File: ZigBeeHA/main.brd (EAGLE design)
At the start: 100 x 80 mm, 12 parts, among them IC1 REG1117

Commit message: 1st completion
1st completion
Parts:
- added F1: (no value), fuse:GSH15
- added PAD4, PAD5, PAD6: (no value), wirepad:2,54/0,8
- added PAD7: +5V, wirepad:2,54/0,8
- added PAD8: GND, wirepad:2,54/0,8
- added PAD9: +3.3V, wirepad:2,54/0,8
- added SV4: (no value), con-lstb:MA03-1
- added X1: 5202-03-N-02, con-ebyelectro:5202-03-N-02
- PAD1: value +5V -> AC-; device wirepad:2,54/0,8 -> wirepad:2,54/1,0
- PAD2: value GND -> AC+; device wirepad:2,54/0,8 -> wirepad:2,54/1,0
- PAD3: value +3.3V -> (none)
- moved PAD3 83.3 mm to (-6.35, -30.5)
- moved PAD2 75.5 mm to (-6.35, -20.3)
- moved PAD1 54.6 mm to (-6.35, -15.2)
- renumbered C5 to C4
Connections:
- new net AC+: X1.3
- new net LAMP: X1.2
- new net N$1: PAD1.1, PAD3.1
- new net N$2: F1.1, PAD2.1
- new net N$3: F1.2, PAD4.1
- net +5V: now also PAD5.1, PAD7.1, SV4.1; no longer PAD1.1
- net GND: now also PAD6.1, PAD8.1, SV4.2; no longer PAD2.1
- net PC6/MODE/DIO0: now also SV4.3
- net VCC: now also PAD9.1; no longer PAD3.1
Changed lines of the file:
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@@
 <element name="C3" library="rcl" package="SANYO-OSCON_SMD_A5" value="4.7uF" x="13.97" y="44.45" rot="R180"/>
 <element name="R1" library="rcl" package="M1206" value="10K" x="15.24" y="52.07" rot="R180"/>
-<element name="PAD1" library="wirepad" package="2,54/0,8" value="+5V" x="5.08" y="38.1"/>
-<element name="PAD2" library="wirepad" package="2,54/0,8" value="GND" x="60.96" y="13.97"/>
-<element name="PAD3" library="wirepad" package="2,54/0,8" value="+3.3V" x="5.08" y="52.07"/>
+<element name="PAD7" library="wirepad" package="2,54/0,8" value="+5V" x="5.08" y="38.1"/>
+<element name="PAD8" library="wirepad" package="2,54/0,8" value="GND" x="60.96" y="13.97"/>
+<element name="PAD9" library="wirepad" package="2,54/0,8" value="+3.3V" x="5.08" y="52.07"/>
 <element name="SV1" library="con-lstb" package="MA13-1" value="" x="35.56" y="36.83" rot="R270">
 <attribute name="OC_NEWARK" value="unknown" x="8.89" y="6.35" size="1.778" layer="27" rot="R270" display="off"/>
@@
 </element>
 <element name="C1" library="rcl" package="SANYO-OSCON_SMD_A5" value="4.7uF" x="21.59" y="27.94" rot="R90"/>
-<element name="C5" library="rcl" package="C1206" value="10uF" x="21.59" y="50.8" rot="R270"/>
+<element name="C4" library="rcl" package="C1206" value="10uF" x="21.59" y="50.8" rot="R270"/>
+<element name="F1" library="fuse" package="GSH15" value="" x="12.7" y="-6.35">
+<attribute name="OC_NEWARK" value="02P0318" x="12.7" y="-6.35" size="1.778" layer="27" display="off"/>
+<attribute name="MPN" value="64900001039" x="12.7" y="-6.35" size="1.778" layer="27" display="off"/>
+<attribute name="MF" value="" x="12.7" y="-6.35" size="1.778" layer="27" display="off"/>
+<attribute name="OC_FARNELL" value="1271673" x="12.7" y="-6.35" size="1.778" layer="27" display="off"/>
+</element>
+<element name="PAD1" library="wirepad" package="2,54/1,0" value="AC-" x="-6.35" y="-15.24"/>
+<element name="PAD2" library="wirepad" package="2,54/1,0" value="AC+" x="-6.35" y="-20.32"/>
+<element name="PAD3" library="wirepad" package="2,54/0,8" value="" x="-6.35" y="-30.48"/>
+<element name="PAD4" library="wirepad" package="2,54/0,8" value="" x="-6.35" y="-35.56"/>
+<element name="PAD5" library="wirepad" package="2,54/0,8" value="" x="-6.35" y="-40.64"/>
+<element name="PAD6" library="wirepad" package="2,54/0,8" value="" x="-6.35" y="-45.72"/>
+<element name="SV4" library="con-lstb" package="MA03-1" value="" x="-2.54" y="-50.8">
+<attribute name="OC_NEWARK" value="unknown" x="-2.54" y="-50.8" size="1.778" layer="27" display="off"/>
+<attribute name="MPN" value="" x="-2.54" y="-50.8" size="1.778" layer="27" display="off"/>
+<attribute name="MF" value="" x="-2.54" y="-50.8" size="1.778" layer="27" display="off"/>
+<attribute name="OC_FARNELL" value="unknown" x="-2.54" y="-50.8" size="1.778" layer="27" display="off"/>
+</element>
+<element name="X1" library="con-ebyelectro" package="5202-03-N-02" value="5202-03-N-02" x="6.35" y="-60.96">
+<attribute name="OC_NEWARK" value="unknown" x="6.35" y="-60.96" size="1.778" layer="27" display="off"/>
+<attribute name="MPN" value="" x="6.35" y="-60.96" size="1.778" layer="27" display="off"/>
+<attribute name="MF" value="" x="6.35" y="-60.96" size="1.778" layer="27" display="off"/>
+<attribute name="OC_FARNELL" value="unknown" x="6.35" y="-60.96" size="1.778" layer="27" display="off"/>
+</element>
 </elements>
 <signals>
@@
 <contactref element="C2" pad="+"/>
 <contactref element="IC1" pad="3"/>
-<contactref element="PAD1" pad="1"/>
+<contactref element="PAD7" pad="1"/>
+<contactref element="PAD5" pad="1"/>
+<contactref element="SV4" pad="1"/>
+<wire x1="-6.35" y1="-40.64" x2="-5.08" y2="-50.8" width="0" layer="19" extent="1-1"/>
+<wire x1="12.17" y1="26.67" x2="-6.35" y2="-40.64" width="0" layer="19" extent="1-1"/>
+<wire x1="11.6586" y1="38.7096" x2="12.17" y2="26.67" width="0" layer="19" extent="1-1"/>
 <wire x1="5.08" y1="38.1" x2="11.6586" y2="38.7096" width="0" layer="19" extent="1-1"/>
-<wire x1="12.17" y1="26.67" x2="11.6586" y2="38.7096" width="0" layer="19" extent="1-1"/>
 </signal>
 <signal name="GND">
@@
 <contactref element="C3" pad="-"/>
 <contactref element="IC1" pad="1"/>
-<contactref element="PAD2" pad="1"/>
+<contactref element="PAD8" pad="1"/>
 <contactref element="SV1" pad="1"/>
 <contactref element="SV1" pad="13"/>
@@
 <contactref element="C1" pad="-"/>
 <wire x1="15.24" y1="39.37" x2="16.2306" y2="38.7096" width="0.254" layer="1"/>
-<contactref element="C5" pad="2"/>
+<contactref element="C4" pad="2"/>
+<contactref element="PAD6" pad="1"/>
+<contactref element="SV4" pad="2"/>
 <wire x1="35.56" y1="52.07" x2="60.96" y2="52.07" width="0" layer="19" extent="1-1"/>
 <wire x1="21.59" y1="49.4" x2="35.56" y2="52.07" width="0" layer="19" extent="1-1"/>
@@
 <wire x1="60.96" y1="21.59" x2="55.88" y2="21.59" width="0" layer="19" extent="1-1"/>
 <wire x1="60.96" y1="13.97" x2="60.96" y2="21.59" width="0" layer="19" extent="1-1"/>
+<wire x1="-6.35" y1="-45.72" x2="15.77" y2="26.67" width="0" layer="19" extent="1-1"/>
+<wire x1="-2.54" y1="-50.8" x2="-6.35" y2="-45.72" width="0" layer="19" extent="1-1"/>
 </signal>
 <signal name="/RESET">
 <contactref element="R1" pad="1"/>
 <contactref element="SV3" pad="2"/>
-<contactref element="C5" pad="1"/>
+<contactref element="C4" pad="1"/>
 <wire x1="21.59" y1="52.2" x2="60.96" y2="24.13" width="0" layer="19" extent="1-1"/>
 <wire x1="16.64" y1="52.07" x2="21.59" y2="52.2" width="0" layer="19" extent="1-1"/>
@@
 <signal name="PC6/MODE/DIO0">
 <contactref element="SV1" pad="3"/>
+<contactref element="SV4" pad="3"/>
+<wire x1="0" y1="-50.8" x2="35.56" y2="46.99" width="0" layer="19" extent="1-1"/>
 </signal>
 <signal name="PC7/DTR/DIO1">
@@
 <contactref element="C3" pad="+"/>
 <contactref element="R1" pad="2"/>
-<contactref element="PAD3" pad="1"/>
+<contactref element="PAD9" pad="1"/>
 <contactref element="C1" pad="+"/>
 <contactref element="SV1" pad="12"/>
@@
 <wire x1="35.56" y1="24.13" x2="21.59" y2="29.74" width="0" layer="19" extent="1-1"/>
 </signal>
+<signal name="N$1">
+<contactref element="PAD1" pad="1"/>
+<contactref element="PAD3" pad="1"/>
+<wire x1="-6.35" y1="-15.24" x2="-6.35" y2="-30.48" width="0" layer="19" extent="1-1"/>
+</signal>
+<signal name="N$2">
+<contactref element="F1" pad="1"/>
+<contactref element="PAD2" pad="1"/>
+<wire x1="5.08" y1="-6.35" x2="-6.35" y2="-20.32" width="0" layer="19" extent="1-1"/>
+</signal>
+<signal name="N$3">
+<contactref element="F1" pad="2"/>
+<contactref element="PAD4" pad="1"/>
+<wire x1="20.32" y1="-6.35" x2="-6.35" y2="-35.56" width="0" layer="19" extent="1-1"/>
+</signal>
+<signal name="LAMP">
+<contactref element="X1" pad="2"/>
+</signal>
+<signal name="AC+">
+<contactref element="X1" pad="3"/>
+</signal>
 </signals>

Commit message: Merge to Schematics
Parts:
- added C5: 4.7uF, rcl:SANYO-OSCON_SMD_A5
- added SV5, SV6: (no value), con-lstb:MA13-1
- added SV7: (no value), con-lstb:MA08-1
- added SV8, SV9: (no value), con-lstb:MA12-1
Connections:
- removed net PB1/TXD: SV3.6
- removed net PB2/RXD: SV3.5
- new net A0: SV9.5
- new net A1: SV9.6
- new net A2: SV9.7
- new net A3: SV9.8
- new net D10: SV9.1
- new net D2: SV8.8
- new net D3: SV8.7
- new net D4: SV8.6
- new net D5: SV8.5
- new net D6: SV8.4
- new net D7: SV8.3
- new net D8: SV8.2
- new net D9: SV8.1
- new net GND1: SV6.1, SV6.13
- new net MISO: SV9.3
- new net MOSI: SV9.2
- new net RAW: SV9.12
- new net RESET: SV8.10, SV9.10
- new net RXD: SV3.5, SV5.1
- new net RXI: SV8.11
- new net SCK: SV9.4
- new net TXD: SV3.6, SV5.2
- new net TXO: SV8.12
- net +5V: now also SV9.9
- net GND: now also C5.-, SV5.13, SV8.9, SV9.11
- net PA3/NSSEL/DIO8: now also SV4.3
- net PC6/MODE/DIO0: no longer SV4.3
- net VCC: now also C5.+, SV5.12
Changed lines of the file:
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@@
 <attribute name="OC_FARNELL" value="unknown" x="6.35" y="-60.96" size="1.778" layer="27" display="off"/>
+</element>
+<element name="SV5" library="con-lstb" package="MA13-1" value="" x="8.89" y="-74.93">
+<attribute name="OC_NEWARK" value="unknown" x="8.89" y="-74.93" size="1.778" layer="27" display="off"/>
+<attribute name="MPN" value="" x="8.89" y="-74.93" size="1.778" layer="27" display="off"/>
+<attribute name="MF" value="" x="8.89" y="-74.93" size="1.778" layer="27" display="off"/>
+<attribute name="OC_FARNELL" value="unknown" x="8.89" y="-74.93" size="1.778" layer="27" display="off"/>
+</element>
+<element name="SV6" library="con-lstb" package="MA13-1" value="" x="8.89" y="-82.55">
+<attribute name="OC_NEWARK" value="unknown" x="8.89" y="-82.55" size="1.778" layer="27" display="off"/>
+<attribute name="MPN" value="" x="8.89" y="-82.55" size="1.778" layer="27" display="off"/>
+<attribute name="MF" value="" x="8.89" y="-82.55" size="1.778" layer="27" display="off"/>
+<attribute name="OC_FARNELL" value="unknown" x="8.89" y="-82.55" size="1.778" layer="27" display="off"/>
+</element>
+<element name="C5" library="rcl" package="SANYO-OSCON_SMD_A5" value="4.7uF" x="-3.81" y="-99.06"/>
+<element name="SV7" library="con-lstb" package="MA08-1" value="" x="2.54" y="-107.95">
+<attribute name="OC_NEWARK" value="unknown" x="2.54" y="-107.95" size="1.778" layer="27" display="off"/>
+<attribute name="MPN" value="" x="2.54" y="-107.95" size="1.778" layer="27" display="off"/>
+<attribute name="MF" value="" x="2.54" y="-107.95" size="1.778" layer="27" display="off"/>
+<attribute name="OC_FARNELL" value="unknown" x="2.54" y="-107.95" size="1.778" layer="27" display="off"/>
+</element>
+<element name="SV8" library="con-lstb" package="MA12-1" value="" x="7.62" y="-115.57">
+<attribute name="OC_NEWARK" value="unknown" x="7.62" y="-115.57" size="1.778" layer="27" display="off"/>
+<attribute name="MPN" value="" x="7.62" y="-115.57" size="1.778" layer="27" display="off"/>
+<attribute name="MF" value="" x="7.62" y="-115.57" size="1.778" layer="27" display="off"/>
+<attribute name="OC_FARNELL" value="unknown" x="7.62" y="-115.57" size="1.778" layer="27" display="off"/>
+</element>
+<element name="SV9" library="con-lstb" package="MA12-1" value="" x="7.62" y="-123.19">
+<attribute name="OC_NEWARK" value="unknown" x="7.62" y="-123.19" size="1.778" layer="27" display="off"/>
+<attribute name="MPN" value="" x="7.62" y="-123.19" size="1.778" layer="27" display="off"/>
+<attribute name="MF" value="" x="7.62" y="-123.19" size="1.778" layer="27" display="off"/>
+<attribute name="OC_FARNELL" value="unknown" x="7.62" y="-123.19" size="1.778" layer="27" display="off"/>
 </element>
 </elements>
@@
 <contactref element="PAD5" pad="1"/>
 <contactref element="SV4" pad="1"/>
+<contactref element="SV9" pad="9"/>
+<wire x1="-5.08" y1="-50.8" x2="13.97" y2="-123.19" width="0" layer="19" extent="1-1"/>
 <wire x1="-6.35" y1="-40.64" x2="-5.08" y2="-50.8" width="0" layer="19" extent="1-1"/>
 <wire x1="12.17" y1="26.67" x2="-6.35" y2="-40.64" width="0" layer="19" extent="1-1"/>
@@
 <contactref element="PAD6" pad="1"/>
 <contactref element="SV4" pad="2"/>
+<contactref element="C5" pad="-"/>
+<contactref element="SV5" pad="13"/>
+<contactref element="SV8" pad="9"/>
+<contactref element="SV9" pad="11"/>
 <wire x1="35.56" y1="52.07" x2="60.96" y2="52.07" width="0" layer="19" extent="1-1"/>
 <wire x1="21.59" y1="49.4" x2="35.56" y2="52.07" width="0" layer="19" extent="1-1"/>
@@
 <wire x1="-6.35" y1="-45.72" x2="15.77" y2="26.67" width="0" layer="19" extent="1-1"/>
 <wire x1="-2.54" y1="-50.8" x2="-6.35" y2="-45.72" width="0" layer="19" extent="1-1"/>
+<wire x1="24.13" y1="-74.93" x2="-2.54" y2="-50.8" width="0" layer="19" extent="1-1"/>
+<wire x1="-5.61" y1="-99.06" x2="24.13" y2="-74.93" width="0" layer="19" extent="1-1"/>
+<wire x1="13.97" y1="-115.57" x2="-5.61" y2="-99.06" width="0" layer="19" extent="1-1"/>
+<wire x1="19.05" y1="-123.19" x2="13.97" y2="-115.57" width="0" layer="19" extent="1-1"/>
 </signal>
 <signal name="/RESET">
@@
 <wire x1="16.64" y1="52.07" x2="21.59" y2="52.2" width="0" layer="19" extent="1-1"/>
 </signal>
-<signal name="PB2/RXD">
-<contactref element="SV3" pad="5"/>
-</signal>
-<signal name="PB1/TXD">
-<contactref element="SV3" pad="6"/>
-</signal>
 <signal name="PB5/ADC0/DIO9">
 <contactref element="SV3" pad="12"/>
@@
 <signal name="PC6/MODE/DIO0">
 <contactref element="SV1" pad="3"/>
-<contactref element="SV4" pad="3"/>
-<wire x1="0" y1="-50.8" x2="35.56" y2="46.99" width="0" layer="19" extent="1-1"/>
 </signal>
 <signal name="PC7/DTR/DIO1">
@@
 <signal name="PA3/NSSEL/DIO8">
 <contactref element="SV1" pad="11"/>
+<contactref element="SV4" pad="3"/>
+<wire x1="0" y1="-50.8" x2="35.56" y2="26.67" width="0" layer="19" extent="1-1"/>
 </signal>
 <signal name="VCC">
@@
 <contactref element="SV1" pad="12"/>
 <contactref element="SV2" pad="1"/>
-<wire x1="38.1" y1="21.59" x2="35.56" y2="24.13" width="0" layer="19" extent="1-16"/>
-<wire x1="40.64" y1="21.59" x2="38.1" y2="21.59" width="0" layer="19" extent="1-16"/>
-<wire x1="12.7" y1="36.83" x2="15.24" y2="36.83" width="0" layer="19" extent="1-16"/>
-<wire x1="12.7" y1="38.1" x2="12.7" y2="36.83" width="0" layer="19" extent="1-16"/>
 <wire x1="12.7" y1="38.1" x2="13.9446" y2="38.7096" width="0.254" layer="1"/>
-<wire x1="12.17" y1="44.45" x2="13.84" y2="52.07" width="0" layer="19" extent="1-1"/>
+<contactref element="C5" pad="+"/>
+<contactref element="SV5" pad="12"/>
+<wire x1="21.59" y1="-74.93" x2="-2.01" y2="-99.06" width="0" layer="19" extent="1-1"/>
+<wire x1="40.64" y1="21.59" x2="21.59" y2="-74.93" width="0" layer="19" extent="1-1"/>
+<wire x1="35.56" y1="24.13" x2="40.64" y2="21.59" width="0" layer="19" extent="1-1"/>
+<wire x1="21.59" y1="29.74" x2="35.56" y2="24.13" width="0" layer="19" extent="1-1"/>
+<wire x1="13.9446" y1="38.7096" x2="21.59" y2="29.74" width="0" layer="19" extent="1-1"/>
+<wire x1="12.17" y1="44.45" x2="13.9446" y2="38.7096" width="0" layer="19" extent="1-1"/>
+<wire x1="13.84" y1="52.07" x2="12.17" y2="44.45" width="0" layer="19" extent="1-1"/>
 <wire x1="5.08" y1="52.07" x2="13.84" y2="52.07" width="0" layer="19" extent="1-1"/>
-<wire x1="13.9446" y1="38.7096" x2="12.17" y2="44.45" width="0" layer="19" extent="1-1"/>
-<wire x1="21.59" y1="29.74" x2="15.24" y2="36.83" width="0" layer="19" extent="1-1"/>
-<wire x1="35.56" y1="24.13" x2="21.59" y2="29.74" width="0" layer="19" extent="1-1"/>
 </signal>
 <signal name="N$1">
@@
 <contactref element="X1" pad="3"/>
 </signal>
+<signal name="GND1">
+<contactref element="SV6" pad="1"/>
+<contactref element="SV6" pad="13"/>
+<wire x1="24.13" y1="-82.55" x2="-6.35" y2="-82.55" width="0" layer="19" extent="1-1"/>
+</signal>
+<signal name="TXD">
+<contactref element="SV3" pad="6"/>
+<contactref element="SV5" pad="2"/>
+<wire x1="-3.81" y1="-74.93" x2="60.96" y2="34.29" width="0" layer="19" extent="1-1"/>
+</signal>
+<signal name="RXD">
+<contactref element="SV3" pad="5"/>
+<contactref element="SV5" pad="1"/>
+<wire x1="-6.35" y1="-74.93" x2="60.96" y2="31.75" width="0" layer="19" extent="1-1"/>
+</signal>
+<signal name="D9">
+<contactref element="SV8" pad="1"/>
+</signal>
+<signal name="D8">
+<contactref element="SV8" pad="2"/>
+</signal>
+<signal name="D7">
+<contactref element="SV8" pad="3"/>
+</signal>
+<signal name="D6">
+<contactref element="SV8" pad="4"/>
+</signal>
+<signal name="D5">
+<contactref element="SV8" pad="5"/>
+</signal>
+<signal name="D4">
+<contactref element="SV8" pad="6"/>
+</signal>
+<signal name="D3">
+<contactref element="SV8" pad="7"/>
+</signal>
+<signal name="D2">
+<contactref element="SV8" pad="8"/>
+</signal>
+<signal name="RESET">
+<contactref element="SV8" pad="10"/>
+<contactref element="SV9" pad="10"/>
+<wire x1="16.51" y1="-115.57" x2="16.51" y2="-123.19" width="0" layer="19" extent="1-1"/>
+</signal>
+<signal name="RXI">
+<contactref element="SV8" pad="11"/>
+</signal>
+<signal name="TXO">
+<contactref element="SV8" pad="12"/>
+</signal>
+<signal name="D10">
+<contactref element="SV9" pad="1"/>
+</signal>
+<signal name="MOSI">
+<contactref element="SV9" pad="2"/>
+</signal>
+<signal name="MISO">
+<contactref element="SV9" pad="3"/>
+</signal>
+<signal name="SCK">
+<contactref element="SV9" pad="4"/>
+</signal>
+<signal name="A0">
+<contactref element="SV9" pad="5"/>
+</signal>
+<signal name="A1">
+<contactref element="SV9" pad="6"/>
+</signal>
+<signal name="A2">
+<contactref element="SV9" pad="7"/>
+</signal>
+<signal name="A3">
+<contactref element="SV9" pad="8"/>
+</signal>
+<signal name="RAW">
+<contactref element="SV9" pad="12"/>
+</signal>
 </signals>

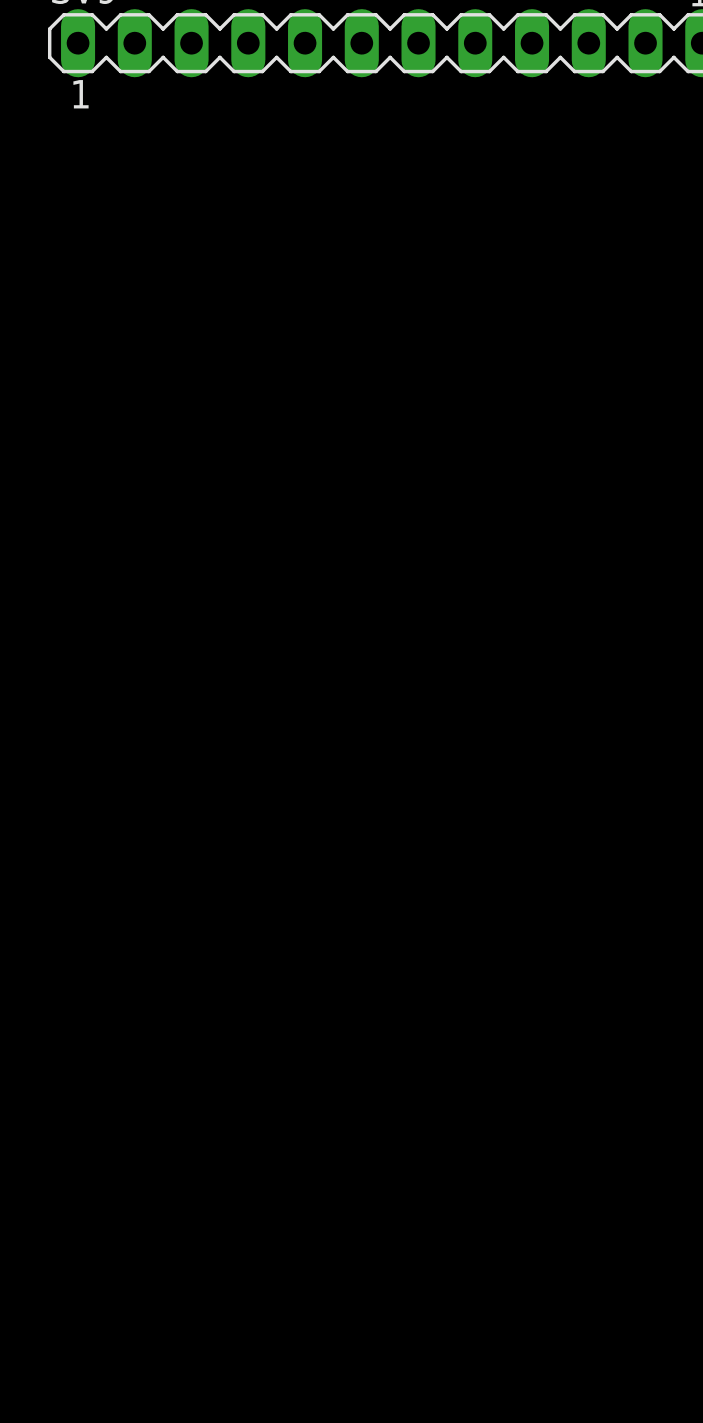
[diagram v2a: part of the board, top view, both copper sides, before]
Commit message: Arduino is added for Servo control
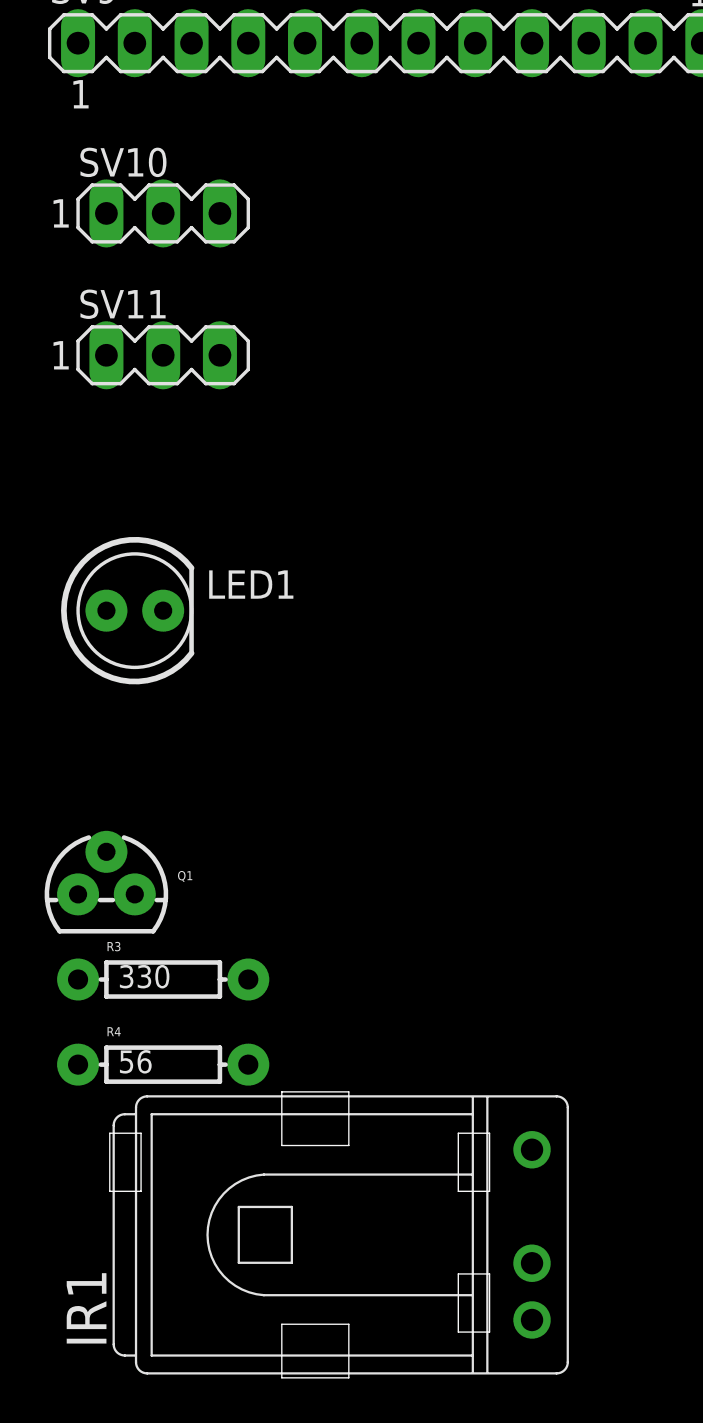
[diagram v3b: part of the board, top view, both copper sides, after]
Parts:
- added IR1: TSOP1730TB1, telefunken:TSOP17_TB1
- added LED1: IR, SparkFun:LED5MM
- added Q1: 2N3904, SparkFun:TO-92
- added R3: 330, SparkFun:AXIAL-0.3
- added R4: 56, SparkFun:AXIAL-0.3
- added SV10, SV11: (no value), con-lstb:MA03-1
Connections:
- net MISO renamed D12_MISO
- net MOSI renamed D11_MOSI
- net SCK renamed D13_SCK
- new net N$5: Q1.2, R3.P$1
- new net N$6: LED1.A, R4.P$2
- new net N$7: LED1.K, Q1.3
- net +5V: now also IR1.VS, R4.P$1, SV10.2, SV11.2
- net D10: now also SV11.3
- net D3: now also R3.P$2
- net D5: now also IR1.VO
- net D9: now also SV10.3
- net GND: now also IR1.GND, Q1.1, SV10.1, SV11.1
- net RXD: no longer SV5.1
- net RXI: now also SV5.1
- net TXD: no longer SV5.2
- net TXO: now also SV5.2
